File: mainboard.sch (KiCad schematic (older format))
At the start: 74 parts, among them J1 Conn_01x06, J2 10118194-0001LF, J4 xf2m-2415-1a, J5 XF2M-1015-1A, J9 Conn_01x02, Q1 RADFET, SW1 KMR231NG LFS, U10 TPS22918-Q1, U11 DRV8830DRC, U3 DRV8830DRC, U4 TPS82740BSIPR, U5 DRV8830DRC, U6 MAX708RESA-T, U7 BMX160, U9 ADS124S06IRHBR

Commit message: updated footprints
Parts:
- J3: renamed from J?; footprint custom-footprints:U.FL-R-SMT-1 -> UFL-R:U.FL-R-SMT-1
- U2: renamed from U?; footprint (none) -> MR25H40:SON127P600X500X90-9N
- U8: renamed from U?; footprint custom-footprints:RFM95PW -> RFM95PW:RFM95PW
- gave numbers to parts that had none: 10
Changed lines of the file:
@@
 COIL6_N
 $Comp
-L MCU_Microchip_SAMD:ATSAMD51J20A-M U?
+L MCU_Microchip_SAMD:ATSAMD51J20A-M U1
 U 1 1 5F37375A
 P 3150 8300
-F 0 "U?" H 3250 7350 50  0000 C CNN
+F 0 "U1" H 3250 7350 50  0000 C CNN
 F 1 "ATSAMD51J20A-M" H 3300 7200 50  0000 C CNN
 F 2 "Package_DFN_QFN:QFN-64-1EP_9x9mm_P0.5mm_EP4.7x4.7mm" H 3150 8300 50  0001 C CIN
@@
 $EndComp
 $Comp
-L power:+3V3 #PWR?
+L power:+3V3 #PWR0107
 U 1 1 5F3F5D57
 P 3350 6300
-F 0 "#PWR?" H 3350 6150 50  0001 C CNN
+F 0 "#PWR0107" H 3350 6150 50  0001 C CNN
 F 1 "+3V3" H 3365 6473 50  0000 C CNN
 F 2 "" H 3350 6300 50  0001 C CNN
@@
 $EndComp
 $Comp
-L mainboard-rescue:L_Small-Device L?
+L mainboard-rescue:L_Small-Device L1
 U 1 1 5F404DFD
 P 2750 6400
-F 0 "L?" V 2700 6400 50  0000 C CNN
+F 0 "L1" V 2700 6400 50  0000 C CNN
 F 1 "10uH" V 2850 6400 50  0000 C CNN
 F 2 "Inductor_SMD:L_0805_2012Metric" H 2750 6400 50  0001 C CNN
@@
 	2850 6300 2750 6300
 $Comp
-L mainboard-rescue:C_Small-Device C?
+L mainboard-rescue:C_Small-Device C9
 U 1 1 5F4200AB
 P 2200 6200
-F 0 "C?" H 2050 6250 50  0000 L CNN
+F 0 "C9" H 2050 6250 50  0000 L CNN
 F 1 "10uF" H 1950 6150 50  0000 L CNN
 F 2 "Capacitor_SMD:C_0402_1005Metric" H 2200 6200 50  0001 C CNN
@@
 $EndComp
 $Comp
-L mainboard-rescue:C_Small-Device C?
+L mainboard-rescue:C_Small-Device C10
 U 1 1 5F420663
 P 2400 6200
-F 0 "C?" H 2492 6246 50  0000 L CNN
+F 0 "C10" H 2492 6246 50  0000 L CNN
 F 1 "1uF" H 2492 6155 50  0000 L CNN
 F 2 "Capacitor_SMD:C_0402_1005Metric" H 2400 6200 50  0001 C CNN
@@
 Connection ~ 2850 6300
 $Comp
-L power:GND #PWR?
+L power:GND #PWR0108
 U 1 1 5F44DAEA
 P 2200 6300
-F 0 "#PWR?" H 2200 6050 50  0001 C CNN
+F 0 "#PWR0108" H 2200 6050 50  0001 C CNN
 F 1 "GND" H 2205 6127 50  0000 C CNN
 F 2 "" H 2200 6300 50  0001 C CNN
@@
 $EndComp
 $Comp
-L power:GND #PWR?
+L power:GND #PWR0109
 U 1 1 5F44E243
 P 2400 6300
-F 0 "#PWR?" H 2400 6050 50  0001 C CNN
+F 0 "#PWR0109" H 2400 6050 50  0001 C CNN
 F 1 "GND" H 2405 6127 50  0000 C CNN
 F 2 "" H 2400 6300 50  0001 C CNN
@@
 $EndComp
 $Comp
-L power:GND #PWR?
+L power:GND #PWR0111
 U 1 1 5F450F3C
 P 3150 10100
-F 0 "#PWR?" H 3150 9850 50  0001 C CNN
+F 0 "#PWR0111" H 3150 9850 50  0001 C CNN
 F 1 "GND" H 3155 9927 50  0000 C CNN
 F 2 "" H 3150 10100 50  0001 C CNN
@@
 $EndComp
 $Comp
-L power:GND #PWR?
+L power:GND #PWR0112
 U 1 1 5F4514FB
 P 3250 10100
-F 0 "#PWR?" H 3250 9850 50  0001 C CNN
+F 0 "#PWR0112" H 3250 9850 50  0001 C CNN
 F 1 "GND" H 3255 9927 50  0000 C CNN
 F 2 "" H 3250 10100 50  0001 C CNN
@@
 	3350 6450 3350 6300
 $Comp
-L mainboard-rescue:RFM98PW-symbols U?
+L mainboard-rescue:RFM98PW-symbols U8
 U 1 1 5F33BDE8
 P 14900 4950
-F 0 "U?" H 15000 4370 59  0000 C CNN
+F 0 "U8" H 15000 4370 59  0000 C CNN
 F 1 "RFM98PW-symbols" H 15000 4500 50  0001 C CNN
-F 2 "custom-footprints:RFM95PW" H 15000 4400 50  0001 C CNN
+F 2 "RFM95PW:RFM95PW" H 15000 4400 50  0001 C CNN
 F 3 "" H 14900 4950 50  0001 C CNN
 	1    14900 4950
@@
 RF2_CS
 $Comp
-L mainboard-rescue:R_US-Device R?
+L mainboard-rescue:R_US-Device R18
 U 1 1 5F341073
 P 13900 4700
-F 0 "R?" H 14050 4750 50  0000 C CNN
+F 0 "R18" H 14050 4750 50  0000 C CNN
 F 1 "10K" H 14050 4650 50  0000 C CNN
 F 2 "Resistor_SMD:R_0402_1005Metric" V 13940 4690 50  0001 C CNN
@@
 	14400 4550 14400 4650
 $Comp
-L power:+3V3 #PWR?
+L power:+3V3 #PWR0113
 U 1 1 5F3BAC92
 P 14400 4550
-F 0 "#PWR?" H 14400 4400 50  0001 C CNN
+F 0 "#PWR0113" H 14400 4400 50  0001 C CNN
 F 1 "+3V3" H 14415 4723 50  0000 C CNN
 F 2 "" H 14400 4550 50  0001 C CNN
@@
 RF_BUSY
 $Comp
-L power:GND #PWR?
+L power:GND #PWR0115
 U 1 1 5F3BC393
 P 15600 5350
-F 0 "#PWR?" H 15600 5100 50  0001 C CNN
+F 0 "#PWR0115" H 15600 5100 50  0001 C CNN
 F 1 "GND" H 15605 5177 50  0000 C CNN
 F 2 "" H 15600 5350 50  0001 C CNN
@@
 $EndComp
 $Comp
-L mainboard-rescue:U.FL-R-SMT-1-symbols J?
+L mainboard-rescue:U.FL-R-SMT-1-symbols J3
 U 1 1 5F3BC982
 P 16000 4400
-F 0 "J?" H 16400 4665 50  0000 C CNN
+F 0 "J3" H 16400 4665 50  0000 C CNN
 F 1 "U.FL-R-SMT-1" H 16400 4574 50  0000 C CNN
-F 2 "custom-footprints:U.FL-R-SMT-1" H 16650 4500 50  0001 L CNN
+F 2 "UFL-R:U.FL-R-SMT-1" H 16650 4500 50  0001 L CNN
 F 3 "https://www.hirose.co.jp/cataloge_hp/ed_UFL_20141014.pdf" H 16650 4400 50  0001 L CNN
 F 4 "" H 16650 4300 50  0001 L CNN "Description"
@@
 $EndComp
 $Comp
-L power:GND #PWR?
+L power:GND #PWR0119
 U 1 1 5F3BD635
 P 16100 4700
-F 0 "#PWR?" H 16100 4450 50  0001 C CNN
+F 0 "#PWR0119" H 16100 4450 50  0001 C CNN
 F 1 "GND" H 16105 4527 50  0000 C CNN
 F 2 "" H 16100 4700 50  0001 C CNN
@@
 	1150 9900 2450 9900
 $Comp
-L mainboard-rescue:R_US-Device R?
+L mainboard-rescue:R_US-Device R15
 U 1 1 5F7F827A
 P 1550 9350
-F 0 "R?" H 1650 9400 50  0000 C CNN
+F 0 "R15" H 1650 9400 50  0000 C CNN
 F 1 "10K" H 1650 9300 50  0000 C CNN
 F 2 "Resistor_SMD:R_0402_1005Metric" V 1590 9340 50  0001 C CNN
@@
 	1550 9200 2450 9200
 $Comp
-L power:GND #PWR?
+L power:GND #PWR0120
 U 1 1 5F7F888E
 P 1550 9500
-F 0 "#PWR?" H 1550 9250 50  0001 C CNN
+F 0 "#PWR0120" H 1550 9250 50  0001 C CNN
 F 1 "GND" H 1555 9327 50  0000 C CNN
 F 2 "" H 1550 9500 50  0001 C CNN
@@
 	1000 9200 1550 9200
 $Comp
-L mainboard-rescue:C_Small-Device C?
+L mainboard-rescue:C_Small-Device C2
 U 1 1 5F850592
 P 600 8650
-F 0 "C?" H 600 8750 50  0000 L CNN
+F 0 "C2" H 600 8750 50  0000 L CNN
 F 1 "0.1uF" H 600 8550 50  0000 L CNN
 F 2 "Capacitor_SMD:C_0402_1005Metric" H 600 8650 50  0001 C CNN
@@
 Connection ~ 1050 8950
 $Comp
-L mainboard-rescue:C_Small-Device C?
+L mainboard-rescue:C_Small-Device C5
 U 1 1 5F93E3EC
 P 1300 7600
-F 0 "C?" H 1200 7700 50  0000 L CNN
+F 0 "C5" H 1200 7700 50  0000 L CNN
 F 1 "0.1uF" H 1050 7550 50  0000 L CNN
 F 2 "Capacitor_SMD:C_0402_1005Metric" H 1300 7600 50  0001 C CNN
@@
 $EndComp
 $Comp
-L mainboard-rescue:R_US-Device R?
+L mainboard-rescue:R_US-Device R16
 U 1 1 5F59D65A
 P 4550 8950
-F 0 "R?" H 4650 8900 50  0000 C CNN
+F 0 "R16" H 4650 8900 50  0000 C CNN
 F 1 "10K" H 4650 8850 50  0000 C CNN
 F 2 "Resistor_SMD:R_0402_1005Metric" V 4590 8940 50  0001 C CNN
@@
 	4550 9100 4800 9100
 $Comp
-L mainboard-rescue:R_US-Device R?
+L mainboard-rescue:R_US-Device R17
 U 1 1 5F59DE3C
 P 4700 8850
-F 0 "R?" H 4800 8800 50  0000 C CNN
+F 0 "R17" H 4800 8800 50  0000 C CNN
 F 1 "10K" H 4800 8750 50  0000 C CNN
 F 2 "Resistor_SMD:R_0402_1005Metric" V 4740 8840 50  0001 C CNN
@@
 	4700 9000 4800 9000
 $Comp
-L power:+3V3 #PWR?
+L power:+3V3 #PWR0126
 U 1 1 5F59E868
 P 4700 8700
-F 0 "#PWR?" H 4700 8550 50  0001 C CNN
+F 0 "#PWR0126" H 4700 8550 50  0001 C CNN
 F 1 "+3V3" H 4715 8873 50  0000 C CNN
 F 2 "" H 4700 8700 50  0001 C CNN
@@
 Connection ~ 4700 8700
 $Comp
-L Memory_NVRAM:MR25H40 U?
+L Memory_NVRAM:MR25H40 U2
 U 1 1 5F5B5E9E
 P 6000 7800
-F 0 "U?" H 6000 8381 50  0000 C CNN
+F 0 "U2" H 5700 8200 50  0000 C CNN
 F 1 "MR25H40" H 6000 8290 50  0000 C CNN
-F 2 "" H 6000 7800 50  0001 C CNN
+F 2 "MR25H40:SON127P600X500X90-9N" H 6000 7800 50  0001 C CNN
 F 3 "https://www.everspin.com/file/217/download" H 5700 8100 50  0001 C CNN
 	1    6000 7800
@@
 FLASH_SCK
 $Comp
-L power:+3V3 #PWR?
+L power:+3V3 #PWR0136
 U 1 1 5F5BBCEF
 P 6000 7400
-F 0 "#PWR?" H 6000 7250 50  0001 C CNN
+F 0 "#PWR0136" H 6000 7250 50  0001 C CNN
 F 1 "+3V3" H 6015 7573 50  0000 C CNN
 F 2 "" H 6000 7400 50  0001 C CNN
@@
 $EndComp
 $Comp
-L power:GND #PWR?
+L power:GND #PWR0137
 U 1 1 5F5BC9E4
 P 6000 8200
-F 0 "#PWR?" H 6000 7950 50  0001 C CNN
+F 0 "#PWR0137" H 6000 7950 50  0001 C CNN
 F 1 "GND" H 6005 8027 50  0000 C CNN
 F 2 "" H 6000 8200 50  0001 C CNN
@@
 $EndComp
 $Comp
-L power:GND #PWR?
+L power:GND #PWR0140
 U 1 1 5F5BD27D
 P 5900 8200
-F 0 "#PWR?" H 5900 7950 50  0001 C CNN
+F 0 "#PWR0140" H 5900 7950 50  0001 C CNN
 F 1 "GND" H 5905 8027 50  0000 C CNN
 F 2 "" H 5900 8200 50  0001 C CNN

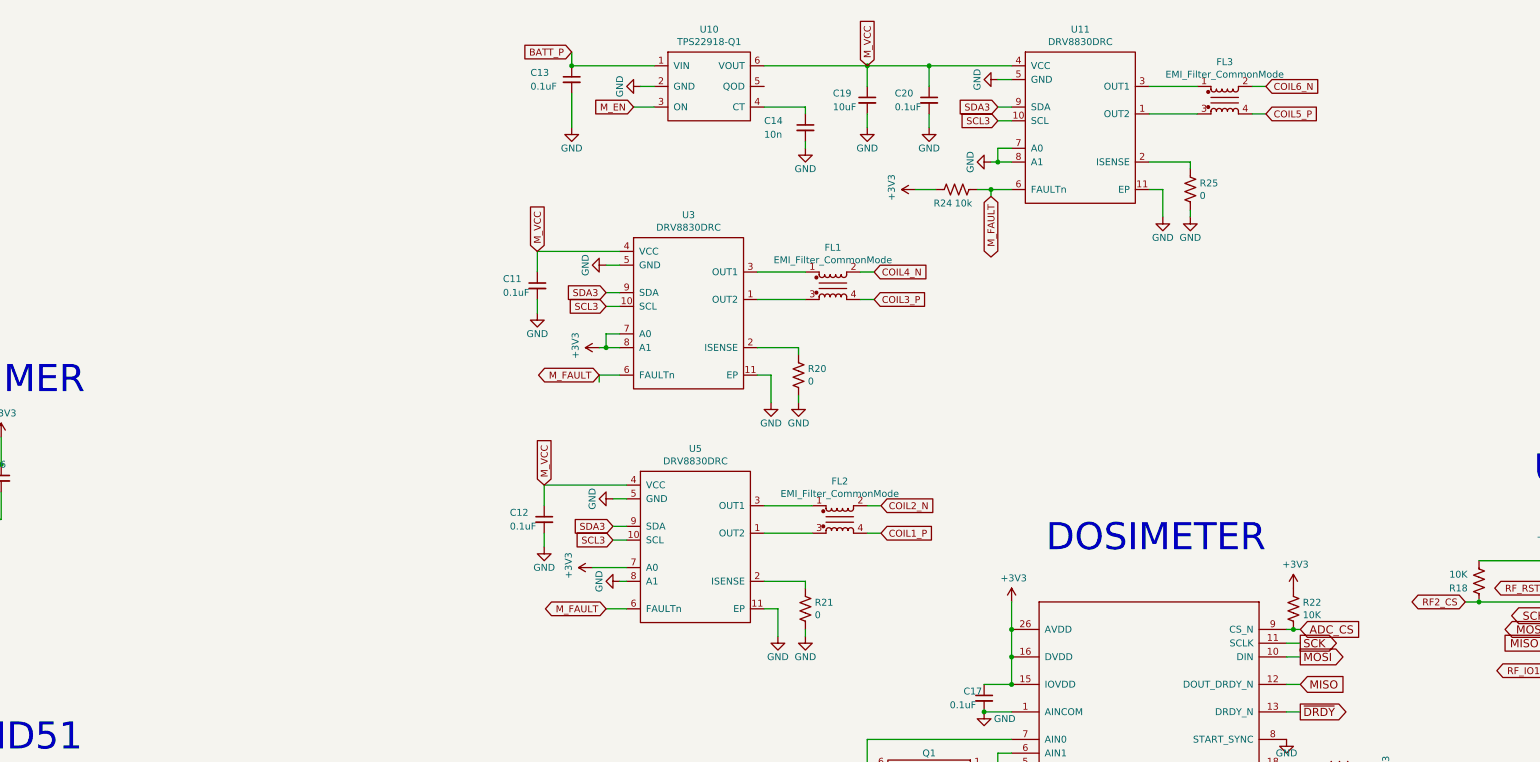
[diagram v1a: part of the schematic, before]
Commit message: power coil drivers directly from battery
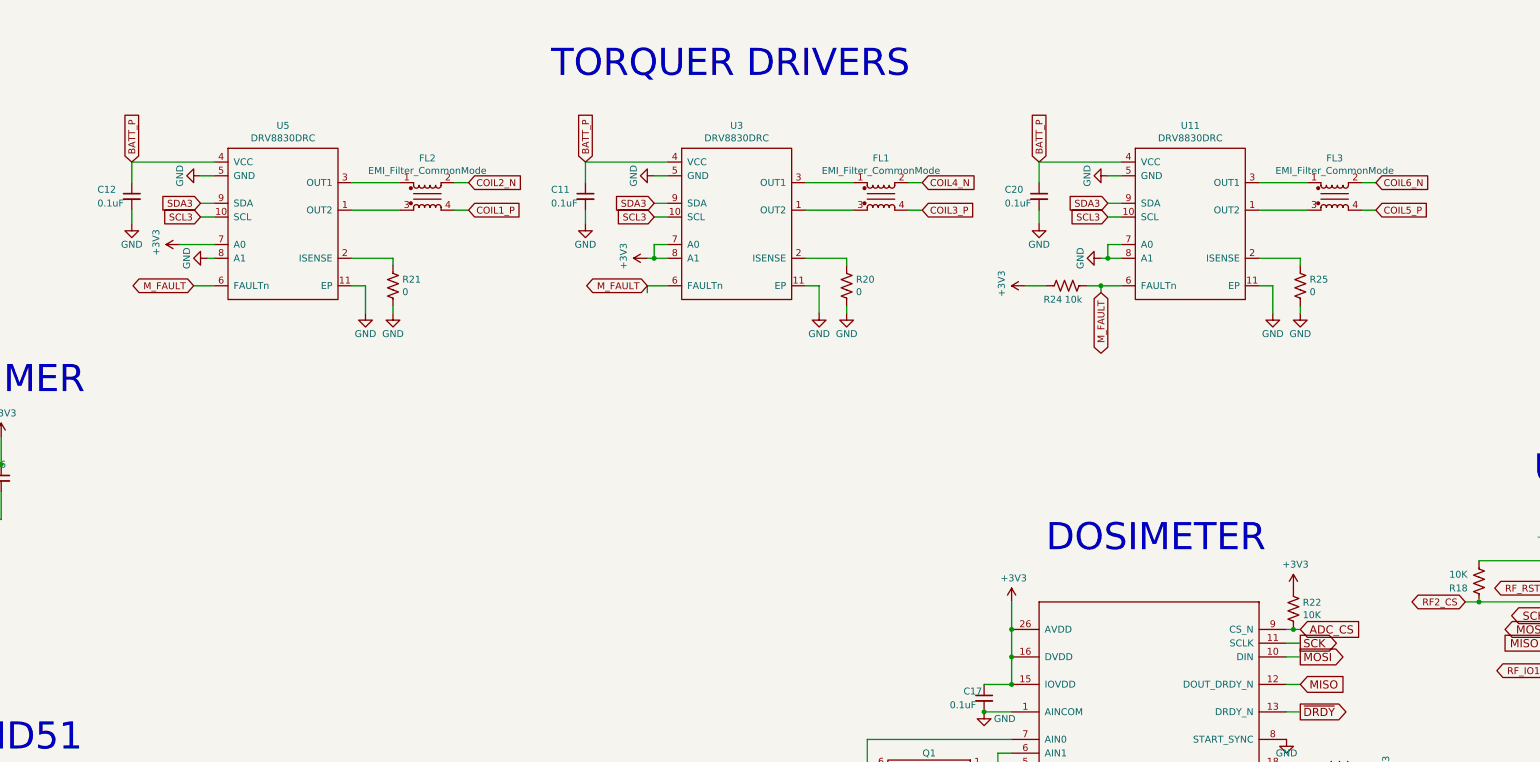
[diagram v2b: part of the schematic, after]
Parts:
- removed C13: 0.1uF, Capacitor_SMD:C_0402_1005Metric, symbol mainboard-rescue:C_Small-Device
- removed C14: 10n, Capacitor_SMD:C_0402_1005Metric, symbol mainboard-rescue:C_Small-Device
- removed C19: 10uF, Capacitor_SMD:C_0805_2012Metric, symbol mainboard-rescue:C_Small-Device
- removed U10: TPS22918-Q1, Package_TO_SOT_SMD:SOT-23-6, symbol mainboard-rescue:TPS22918-Q1-wbraun_ic_lib
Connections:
- net M_VCC is gone; now on net BATT_P: C11.1, C12.1, C20.1, U11.4 (VCC), U3.4 (VCC), U5.4 (VCC)
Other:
- note added: "TORQUER DRIVERS"
- moved on the sheet: C11, C12, C20, FL1, FL2, FL3, R20, R21, R24, R25, U11, U3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

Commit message: beginning layout
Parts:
- removed C2: 0.1uF, Capacitor_SMD:C_0402_1005Metric, symbol mainboard-rescue:C_Small-Device
- removed D3: WS2812B, LED_SMD:LED_WS2812B_PLCC4_5.0x5.0mm_P3.2mm, symbol LED:WS2812B
- removed J2: 10118194-0001LF, custom-footprints:10118194-0001LF, symbol mainboard-rescue:10118194-0001LF-10118194-0001LF
- added C15: 0.1uF, Capacitor_SMD:C_0402_1005Metric, symbol mainboard-rescue:C_Small-Device
- added D1: LED, LED_SMD:LED_0805_2012Metric, symbol Device:LED
- added J2: USB_B_Micro, Connector_USB:USB_Micro-B_Molex_47346-0001, symbol Connector:USB_B_Micro
- added R6: 470R, Resistor_SMD:R_0402_1005Metric, symbol mainboard-rescue:R_US-Device
- J3: renamed from J4; footprint custom-footprints:XF2M-2415-1A -> pycubed:XF2M-2415-1A
- U9: renamed from U8; footprint RFM95PW:RFM95PW -> pycubed:RFM95PW
- renumbered C4 to C1, C8 to C10, C16 to C11, C11 to C13, C18 to C14, C17 to C16, C20 to C17, C6 to C2, C5 to C3, C15 to C4, C1 to C5, C3 to C6, C9 to C7, C7 to C8, C10 to C9, FL2 to FL1, FL1 to FL2, J5 to J4, J9 to J5, J3 to J6, R2 to R1, R16 to R10, R6 to R11, R17 to R12, R5 to R13, R13 to R14, R14 to R15, R21 to R16, R1 to R17, R11 to R18, R12 to R19, R3 to R2, R24 to R21, R25 to R23, R23 to R24, R18 to R25, R9 to R3, R10 to R4, R15 to R5, R8 to R7, R7 to R8, R4 to R9, U7 to U1, U4 to U10, U6 to U2, U1 to U3, U5 to U4, U2 to U5, U3 to U6, U9 to U7, U11 to U8
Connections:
- net +3V3: now also C15.1
- net GND: now also C15.2, D1.1 (K), J2.5 (GND), J2.6 (Shield)
- net USB_D+: now also J2.3 (D+)
- net USB_D-: now also J2.2 (D-)
- net VUSB: now also J2.1 (VBUS)
- net at U3.42 (PA21): now also R6.1
- new net: D1.2 (A), R6.2

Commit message: lots of routing
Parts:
- R16, R20, R23: footprint Resistor_SMD:R_0402_1005Metric -> Resistor_SMD:R_0603_1608Metric
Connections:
- net RF2_CS is gone; now on net RF_CS: R25.1, U9.13 (NSS)
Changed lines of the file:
@@
-	1    0    0    -1
-$EndComp
-$Comp
-L mainboard-rescue:C_Small-Device C14
-U 1 1 5E0A5212
-P 10200 7700
-F 0 "C14" H 10050 7750 50  0000 L CNN
-F 1 "1uF" H 9950 7650 50  0000 L CNN
-F 2 "Capacitor_SMD:C_0402_1005Metric" H 10200 7700 50  0001 C CNN
-F 3 "~" H 10200 7700 50  0001 C CNN
-	1    10200 7700
 	1    0    0    -1
 $EndComp
@@
 F 0 "R23" H 12532 2504 50  0000 R CNN
 F 1 "0" H 12532 2595 50  0000 R CNN
-F 2 "Resistor_SMD:R_0402_1005Metric" V 12640 2540 50  0001 C CNN
+F 2 "Resistor_SMD:R_0603_1608Metric" V 12640 2540 50  0001 C CNN
 F 3 "~" H 12600 2550 50  0001 C CNN
 	1    12600 2550
@@
 	11050 2550 11150 2550
 $Comp
-L mainboard-rescue:C_Small-Device C17
-U 1 1 5E513F3C
-P 10700 1900
-F 0 "C17" H 10450 1950 50  0000 L CNN
-F 1 "0.1uF" H 10450 1850 50  0000 L CNN
-F 2 "Capacitor_SMD:C_0402_1005Metric" H 10700 1900 50  0001 C CNN
-F 3 "~" H 10700 1900 50  0001 C CNN
-	1    10700 1900
-	1    0    0    -1
-$EndComp
-$Comp
 L Device:EMI_Filter_CommonMode FL3
 U 1 1 5E5156C4
@@
 	1    0    0    -1
 $EndComp
-Wire Wire Line
-	10700 2000 10700 2100
 Wire Wire Line
 	11300 1650 10700 1650
@@
 F 0 "R20" H 9232 2504 50  0000 R CNN
 F 1 "0" H 9232 2595 50  0000 R CNN
-F 2 "Resistor_SMD:R_0402_1005Metric" V 9340 2540 50  0001 C CNN
+F 2 "Resistor_SMD:R_0603_1608Metric" V 9340 2540 50  0001 C CNN
 F 3 "~" H 9300 2550 50  0001 C CNN
 	1    9300 2550
@@
 F 0 "R16" H 5932 2504 50  0000 R CNN
 F 1 "0" H 5932 2595 50  0000 R CNN
-F 2 "Resistor_SMD:R_0402_1005Metric" V 6040 2540 50  0001 C CNN
+F 2 "Resistor_SMD:R_0603_1608Metric" V 6040 2540 50  0001 C CNN
 F 3 "~" H 6000 2550 50  0001 C CNN
 	1    6000 2550
@@
 MISO
 Text GLabel 13800 4850 0    50   BiDi ~ 0
-RF2_CS
+RF_CS
 $Comp
 L mainboard-rescue:R_US-Device R25
@@
 Wire Wire Line
 	1300 8850 1100 8850
+Wire Wire Line
+	10700 2000 10700 2100
+$Comp
+L mainboard-rescue:C_Small-Device C14
+U 1 1 5E0A5212
+P 10200 7700
+F 0 "C14" H 10050 7750 50  0000 L CNN
+F 1 "1uF" H 9950 7650 50  0000 L CNN
+F 2 "Capacitor_SMD:C_0402_1005Metric" H 10200 7700 50  0001 C CNN
+F 3 "~" H 10200 7700 50  0001 C CNN
+	1    10200 7700
+	1    0    0    -1
+$EndComp
+$Comp
+L mainboard-rescue:C_Small-Device C17
+U 1 1 5E513F3C
+P 10700 1900
+F 0 "C17" H 10450 1950 50  0000 L CNN
+F 1 "0.1uF" H 10450 1850 50  0000 L CNN
+F 2 "Capacitor_SMD:C_0402_1005Metric" H 10700 1900 50  0001 C CNN
+F 3 "~" H 10700 1900 50  0001 C CNN
+	1    10700 1900
+	1    0    0    -1
+$EndComp
 $EndSCHEMATC
